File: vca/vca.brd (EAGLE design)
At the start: 35.5 x 107.6 mm, 44 parts, among them IC1 OPA4130U, IC2 OPA134D, IC3 OPA2134D, X1 2516-

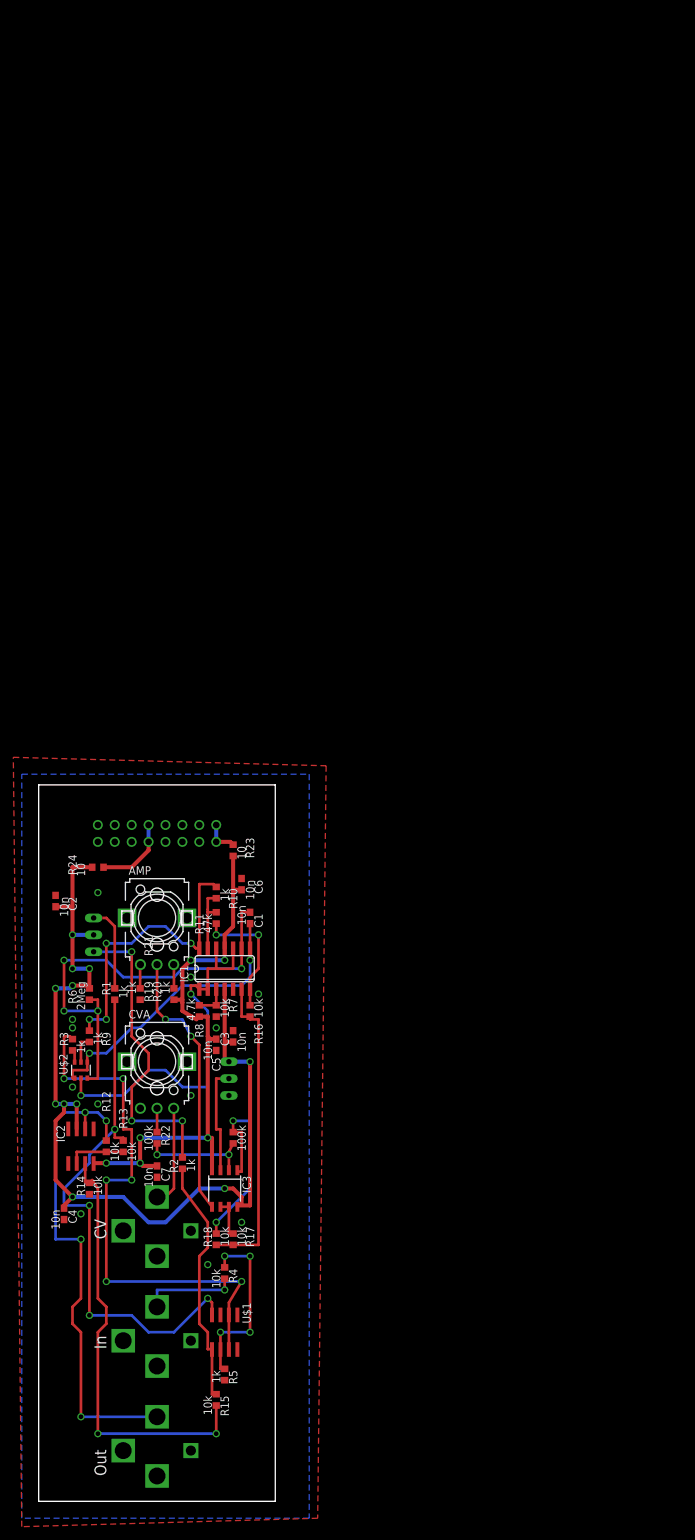
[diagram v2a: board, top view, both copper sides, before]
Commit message: changed the vca to be a 2 board design with a mixer for the input.q
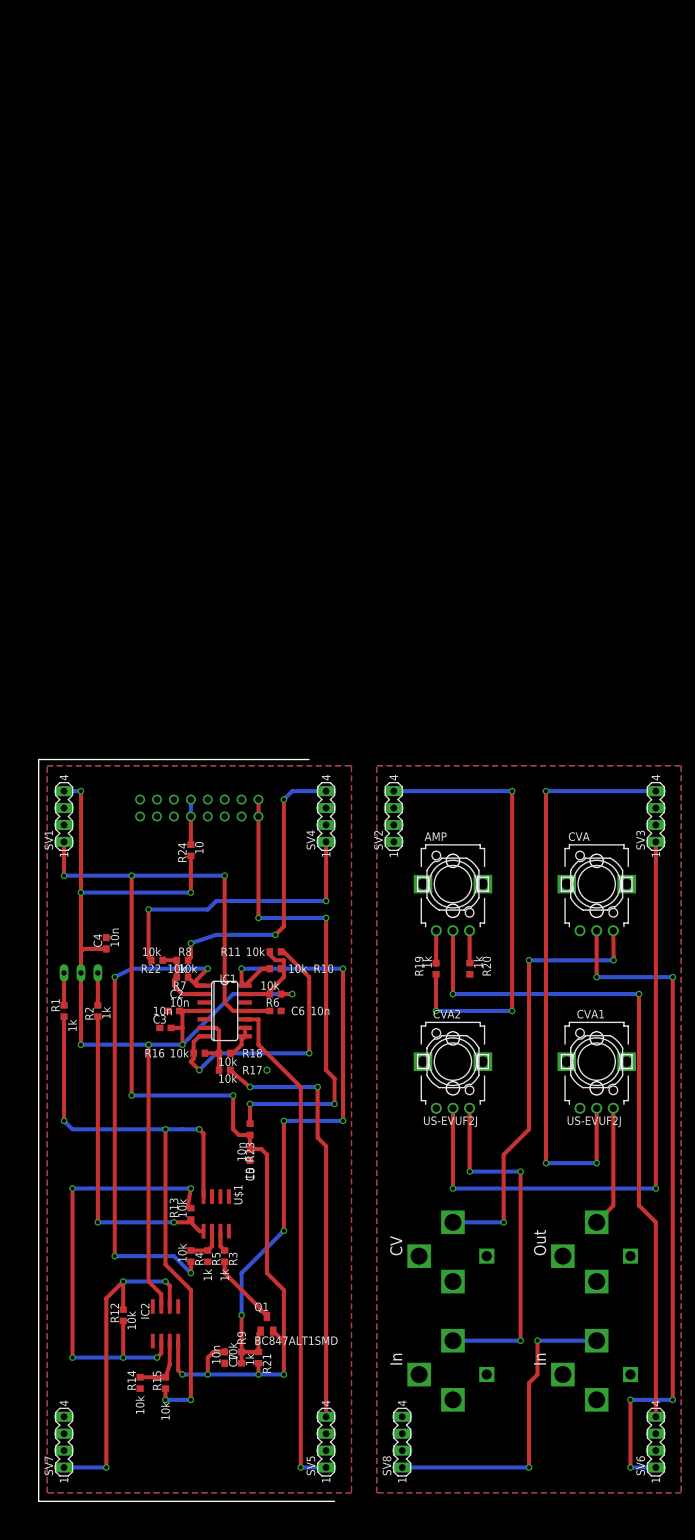
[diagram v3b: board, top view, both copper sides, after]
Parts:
- removed C1: 10n, dan:C0603
- removed IC3: OPA2134D, dan:SOIC8
- removed IN: PJ301BM, dan:PJ301BM
- removed RESP: 10k, dan:RJ9W
- removed U$2: BCM847, dan:SOT457R_PHILIPS
- added CVA1, CVA2: US-EVUF2J, dan:EVUFXJ
- added IN1, IN2: PJ301BM, dan:PJ301BM
- added Q1: BC847ALT1SMD, dan:SOT23
- added SV1, SV2, SV3, SV4, SV5, SV6, SV7, SV8: (no value), dan:MA04-1
- R10, R9: value 1k -> 10k
- R11: value 47k -> 10k
- R21: value 100k -> 1k
- R22: value 100k -> 10k
- R6: value 2Meg -> 10k
- R8: value 4.7k -> 10k
- moved CVA 71.2 mm to (82.5, 92.7)
- moved OUT 67.0 mm to (82.5, 19.1)
- moved R9 53.4 mm to (29.2, 21.6), turned to 270 degrees
- moved AMP 44.7 mm to (61.0, 92.7)
- moved CVIN 44.6 mm to (61.0, 36.8)
- moved R19 44.6 mm to (58.4, 80.0)
- moved R20 44.6 mm to (63.5, 80.0)
- moved R23 42.0 mm to (30.5, 55.9)
- moved C4 41.1 mm to (8.89, 83.8), turned to 90 degrees
- moved R3 39.1 mm to (26.7, 36.8)
- moved R21 33.2 mm to (31.8, 21.6), turned to 270 degrees
- moved R14 30.2 mm to (14.0, 17.8)
- moved C7 29.7 mm to (26.7, 21.6)
- moved IC2 29.5 mm to (17.8, 26.7)
- moved R18 28.0 mm to (26.7, 67.3), turned to 0 degrees
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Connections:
- removed net NEG8: IC1.1, IC1.10, IC1.12, IC1.2, U$2.2
- new net N$29: R22.2, SV4.1
- new net N$31: CVA.2, SV6.1
- new net N$32: AMP.2, SV6.4
- new net N$33: IC1.10, SV5.1
- net +12V: now also R19.1, R6.1, SV1.4, SV2.4; no longer IC3.8, R6.2, RESP.A
- net -12V: now also Q1.2, R21.2, SV1.1, SV2.1; no longer IC3.4, R20.2, R8.2
- net GND: now also CVA1.1, CVA2.1, IC1.12, IC1.3, R20.2, SV1.2, SV1.3, SV2.2, SV2.3, SV3.2, SV3.3, SV4.2, SV4.3, SV5.2, SV5.3, SV6.2, SV6.3, SV7.2, SV7.3, SV7.4, SV8.2, SV8.3, SV8.4; no longer IN.P$1, IN.P$2, IN.P$4, OUT.P$2, R19.1, R7.1, RESP.E
- net N$10: now also IC1.2, R22.1; no longer IC1.3
- net N$11: now also IC1.1, R7.1; no longer IN.P$3
- net N$12: now also R6.2
- net N$18: now also SV7.1; no longer OUT.P$3
- net N$19: now also CVA2.2, SV3.1; no longer IC3.6, IC3.7, R17.2
- net N$21: now also CVA1.2, SV3.4; no longer AMP.2, IC3.5
- net N$24: now also R17.2, SV5.4; no longer IC3.3, RESP.S
- net N$25: now also CVA1.3, IN1.P$3; no longer IC3.2, R21.1, R22.2
- net N$27: now also CVA2.3, IN2.P$3; no longer IC3.1, R18.2, R21.2
- net N$28: now also R8.2, SV4.4; no longer CVA.2, R22.1
- net N$3: now also R13.2; no longer R15.1
- net N$4: now also R15.1; no longer R13.2
- net N$5: now also OUT.P$3, SV8.1; no longer C1.2, IC1.8, U$2.1, U$2.4
- net N$6: now also IC1.8, IC1.9, R18.2; no longer R3.1, U$2.6
- net N$7: now also Q1.3, R3.1; no longer C1.1, IC1.9, R6.1, U$2.3
- net N$8: now also Q1.1, R21.1; no longer U$2.5
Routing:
- net N$31: track 0.00 -> 102.2 mm, vias 0 -> 5
- net N$32: track 0.00 -> 102.0 mm, vias 0 -> 2
- net -12V: track 85.7 -> 180.6 mm, vias 6 -> 9
- net N$19: track 5.93 -> 94.6 mm, vias 0 -> 2
- net N$1: track 83.3 -> 3.16 mm, vias 6 -> 0
- net N$33: track 0.00 -> 75.8 mm, vias 0 -> 1
- net +12V: track 148.3 -> 221.7 mm, vias 11 -> 10
- net N$30: track 5.25 -> 72.1 mm, vias 0 -> 4
- net N$11: track 14.4 -> 76.5 mm, vias 1 -> 4
- net N$16: track 8.73 -> 67.3 mm, vias 0 -> 5
- net NEG8: track 56.4 -> 0.00 mm, vias 2 -> 0
- net N$13: track 65.5 -> 9.35 mm, vias 2 -> 0
- net N$7: track 65.5 -> 10.8 mm, vias 4 -> 0
- net N$26: track 15.1 -> 65.7 mm, vias 0 -> 3
- net N$9: track 44.4 -> 93.5 mm, vias 4 -> 6
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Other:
- board size 35.5 x 107.6 mm -> 44.4 x 111.4 mm

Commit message: finished the vca.  more or less ready.
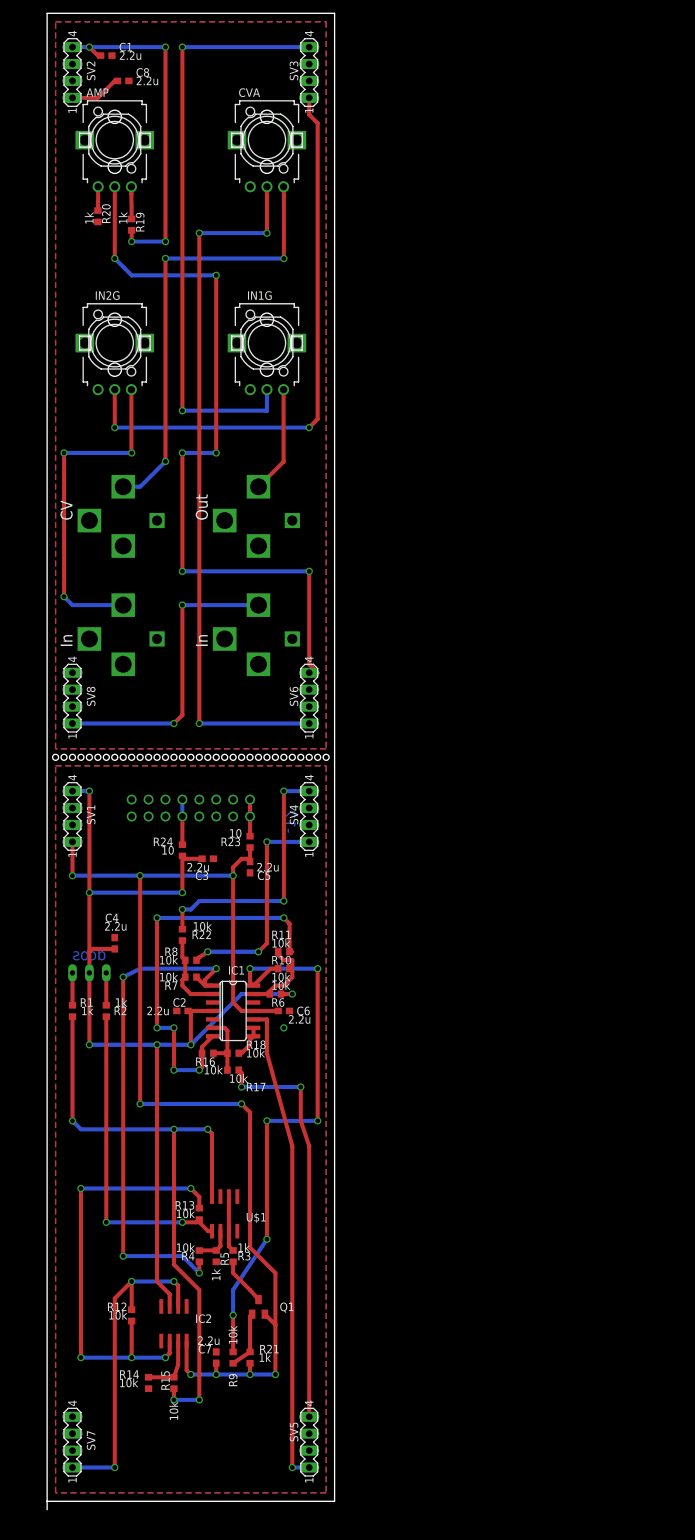
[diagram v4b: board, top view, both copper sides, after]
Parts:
- removed CVA1, CVA2: US-EVUF2J, dan:EVUFXJ
- added C1, C8: 2.2u, dan:C0603
- added IN1G, IN2G: US-EVUF2J, dan:EVUFXJ
- C2, C3, C4, C5, C6, C7: value 10n -> 2.2u
- moved R20 126.1 mm to (7.62, 193.0)
- moved SV6 123.3 mm to (39.4, 120.7)
- moved SV3 123.3 mm to (39.4, 214.6)
- moved AMP 122.8 mm to (10.2, 204.5)
- moved SV8 122.2 mm to (3.81, 120.7)
- moved CVA 122.2 mm to (33.0, 204.5)
- moved SV2 121.7 mm to (3.81, 214.6)
- moved IN1 121.6 mm to (31.8, 147.3)
- moved OUT 121.6 mm to (31.8, 129.5)
- moved CVIN 121.1 mm to (11.4, 147.3)
- moved IN2 121.1 mm to (11.4, 129.5)
- moved R19 120.8 mm to (12.7, 191.8)
- moved C5 43.2 mm to (30.5, 95.2)
- moved R23 43.2 mm to (30.5, 99.1)
- moved C3 26.2 mm to (24.1, 96.5), turned to 0 degrees
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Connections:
- net +12V: now also C1.1
- net -12V: now also C8.1
- net GND: now also C1.2, C8.2, IN1G.1, IN2G.1; no longer CVA1.1, CVA2.1
- net N$19: now also IN2G.2; no longer CVA2.2
- net N$21: now also IN1G.2; no longer CVA1.2
- net N$22: now also AMP.3; no longer AMP.1
- net N$23: now also AMP.1; no longer AMP.3
- net N$25: now also IN1G.3; no longer CVA1.3
- net N$27: now also IN2G.3; no longer CVA2.3
- net N$28: now also SV4.1; no longer SV4.4
- net N$29: now also SV4.4; no longer SV4.1
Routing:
- net N$30: track 72.1 -> 5.50 mm, vias 4 -> 0
- net N$17: track 41.7 -> 60.8 mm, vias 2 -> 6
- net +12V: track 221.7 -> 203.8 mm, vias 10 -> 11
- net N$32: track 102.0 -> 112.7 mm, vias 2 -> 6
- net N$28: track 43.3 -> 33.1 mm
- net N$9: track 93.5 -> 84.4 mm
- net N$19: track 94.6 -> 85.5 mm
- net -12V: track 180.6 -> 185.9 mm
- net N$1: track 3.16 -> 8.36 mm
- net N$31: track 102.2 -> 107.3 mm, vias 5 -> 3
- net N$29: track 43.9 -> 39.0 mm, vias 2 -> 3
- net N$7: track 10.8 -> 7.20 mm
- net N$33: track 75.8 -> 72.4 mm
- net N$8: track 5.80 -> 8.86 mm
- net N$24: track 64.1 -> 61.3 mm
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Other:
- board size 44.4 x 111.4 mm -> 43.2 x 224.8 mm
- board text added: "-12"
- board text added: "dcos"

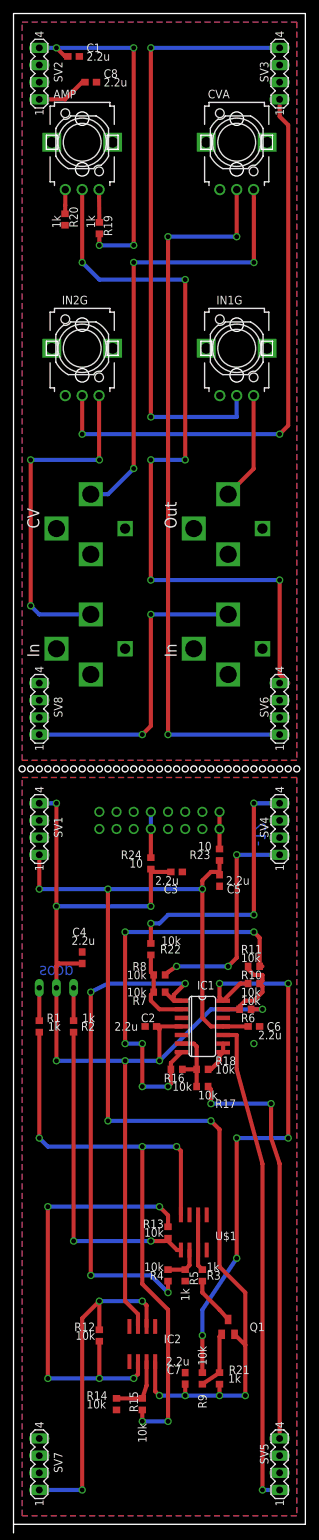
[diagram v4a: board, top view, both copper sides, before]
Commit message: finished vca.  probably needs a series protection resistor on output.
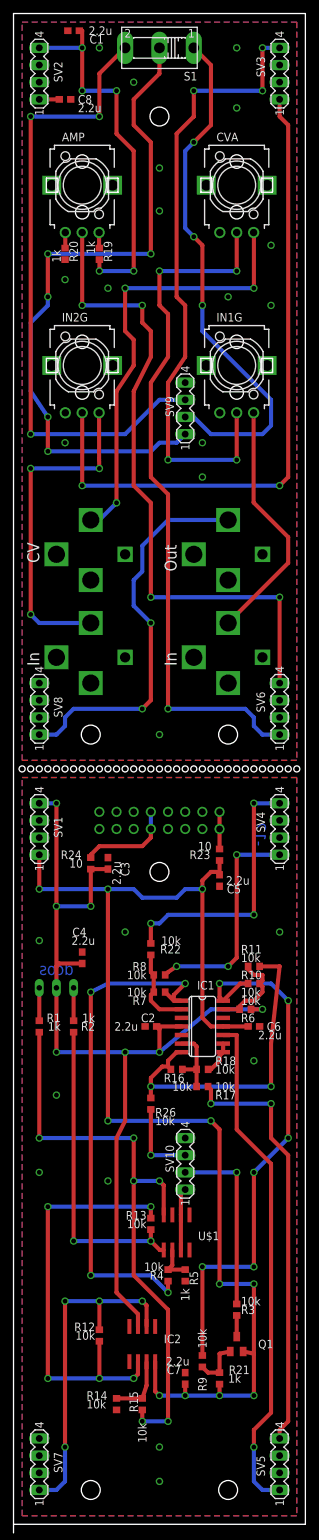
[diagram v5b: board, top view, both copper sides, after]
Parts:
- added R26: 10k, dan:R0603
- added S1: (no value), dan:255SB
- added SV10, SV9: (no value), dan:MA04-1
- R3: value 1k -> 10k
- moved IN1 19.0 mm to (31.8, 128.3)
- moved OUT 14.0 mm to (31.8, 143.5)
- moved C3 10.2 mm to (14.0, 97.8), turned to 90 degrees
- moved R24 8.89 mm to (11.4, 97.8)
- moved R3 7.18 mm to (33.0, 31.8)
- moved AMP 6.35 mm to (10.2, 198.1)
- moved CVA 6.35 mm to (33.0, 198.1)
- moved R20 5.08 mm to (7.62, 188.0)
- moved C8 4.58 mm to (7.62, 210.8)
- moved C1 3.81 mm to (8.89, 221.0), turned to 180 degrees
- moved CVIN 3.81 mm to (11.4, 143.5)
- moved R19 3.81 mm to (12.7, 188.0)
- moved Q1 2.84 mm to (33.0, 26.7)
- moved R13 2.84 mm to (20.3, 44.5)
- moved IN1G 2.54 mm to (33.0, 171.4)
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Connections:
- removed net N$17: IC1.7, R11.2, R16.1
- new net N$35: R3.2, SV10.2
- new net N$36: IC1.7, R11.2, R16.1, R26.1
- new net N$37: S1.2, SV9.1
- new net N$38: R26.2, SV10.3
- new net N$40: S1.1, SV9.2
- new net N$41: S1.3, SV9.3
- net GND: now also SV10.4, SV9.4
- net N$1: now also SV10.1; no longer R3.2
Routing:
- net N$37: track 0.00 -> 100.8 mm, vias 0 -> 5
- net N$41: track 0.00 -> 93.9 mm, vias 0 -> 3
- net N$40: track 0.00 -> 78.0 mm, vias 0 -> 3
- net N$17: track 60.8 -> 0.00 mm, vias 6 -> 0
- net N$36: track 0.00 -> 48.8 mm, vias 0 -> 2
- net N$35: track 0.00 -> 27.1 mm, vias 0 -> 1
- net N$25: track 16.2 -> 36.9 mm
- net N$32: track 112.7 -> 96.8 mm, vias 6 -> 4
- net N$5: track 45.0 -> 58.1 mm
- net N$19: track 85.5 -> 98.2 mm
- net N$38: track 0.00 -> 11.9 mm, vias 0 -> 1
- net +12V: track 203.8 -> 196.1 mm, vias 11 -> 12
- net N$34: track 6.77 -> 14.2 mm
- net N$4: track 94.6 -> 88.2 mm, vias 5 -> 6
- net N$31: track 107.3 -> 103.1 mm
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
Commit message: made a couple post fab vca changes
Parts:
- added R25: 1Meg, dan:R0603
- moved C6 13.1 mm to (29.2, 85.1), turned to 90 degrees
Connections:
- net GND: now also IN1.P$1, IN1.P$2, IN1.P$4, IN2.P$1, IN2.P$2, IN2.P$4, R25.1
- net N$12: now also R25.2
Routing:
- net N$12: track 12.9 -> 16.1 mm
- net -12V: track 186.2 -> 184.0 mm
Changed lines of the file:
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@@
 <attribute name="VALUE" x="34.925" y="95.885" size="1.27" layer="21" font="vector" ratio="15" rot="R180"/>
 </element>
-<element name="C6" library="dan" package="C0603" value="2.2u" x="35.56" y="73.66" smashed="yes">
-<attribute name="NAME" x="37.465" y="73.025" size="1.27" layer="21" font="vector" ratio="15"/>
-<attribute name="VALUE" x="36.195" y="71.755" size="1.27" layer="21" font="vector" ratio="15"/>
+<element name="C6" library="dan" package="C0603" value="2.2u" x="29.21" y="85.09" smashed="yes" rot="R90">
+<attribute name="NAME" x="29.845" y="86.995" size="1.27" layer="21" font="vector" ratio="15"/>
+<attribute name="VALUE" x="29.845" y="85.725" size="1.27" layer="21" font="vector" ratio="15"/>
 </element>
 <element name="C7" library="dan" package="C0603" value="2.2u" x="25.4" y="21.59" smashed="yes" rot="R90">
@@
 <attribute name="NAME" x="23.749" y="52.07" size="1.27" layer="21" font="vector" ratio="15" rot="R90"/>
 <attribute name="VALUE" x="23.749" y="53.975" size="1.27" layer="27" ratio="10" rot="R90"/>
+</element>
+<element name="R25" library="dan" package="R0603" value="1Meg" x="35.56" y="73.66" smashed="yes" rot="R180">
+<attribute name="NAME" x="33.655" y="71.755" size="1.27" layer="21" font="vector" ratio="15"/>
+<attribute name="VALUE" x="33.655" y="70.485" size="1.27" layer="21" font="vector" ratio="15"/>
 </element>
 </elements>
@@
 <via x="13.97" y="182.88" extent="1-16" drill="0.7"/>
 <via x="27.94" y="154.94" extent="1-16" drill="0.7"/>
+<contactref element="IN1" pad="P$4"/>
+<contactref element="IN1" pad="P$2"/>
+<contactref element="IN1" pad="P$1"/>
+<contactref element="IN2" pad="P$4"/>
+<contactref element="IN2" pad="P$1"/>
+<contactref element="IN2" pad="P$2"/>
+<contactref element="R25" pad="1"/>
 <wire x1="22.86" y1="105.41" x2="21.59" y2="116.84" width="0" layer="19" extent="1-1"/>
 </signal>
@@
 <via x="25.4" y="19.05" extent="1-16" drill="0.7"/>
 <wire x1="25.4" y1="19.05" x2="30.48" y2="19.05" width="0.6096" layer="16"/>
-<wire x1="31.0134" y1="73.66" x2="34.71" y2="73.66" width="0.6096" layer="1"/>
 <wire x1="31.0134" y1="73.66" x2="29.21" y2="73.66" width="0.6096" layer="1"/>
 <wire x1="29.21" y1="73.66" x2="27.94" y2="74.93" width="0.6096" layer="1"/>
-<wire x1="27.94" y1="74.93" x2="27.94" y2="93.98" width="0.6096" layer="1"/>
+<wire x1="27.94" y1="74.93" x2="27.94" y2="83.82" width="0.6096" layer="1"/>
 <via x="27.94" y="93.98" extent="1-16" drill="0.7"/>
 <via x="3.81" y="93.98" extent="1-16" drill="0.7"/>
+<wire x1="27.94" y1="83.82" x2="27.94" y2="93.98" width="0.6096" layer="1"/>
 <wire x1="13.97" y1="93.98" x2="3.81" y2="93.98" width="0.6096" layer="16"/>
 <wire x1="3.81" y1="93.98" x2="3.81" y2="99.06" width="0.6096" layer="1"/>
@@
 <wire x1="24.13" y1="92.71" x2="25.4" y2="93.98" width="0.6096" layer="16"/>
 <wire x1="25.4" y1="93.98" x2="27.94" y2="93.98" width="0.6096" layer="16"/>
+<wire x1="29.21" y1="84.24" x2="28.36" y2="84.24" width="0.6096" layer="1"/>
+<wire x1="28.36" y1="84.24" x2="27.94" y2="83.82" width="0.6096" layer="1"/>
 <wire x1="3.81" y1="99.06" x2="3.81" y2="210.82" width="0" layer="19" extent="1-1"/>
 </signal>
@@
 <wire x1="34.29" y1="77.47" x2="35.56" y2="77.47" width="0.6096" layer="1"/>
 <wire x1="35.56" y1="77.47" x2="36.83" y2="78.74" width="0.6096" layer="1"/>
+<contactref element="R25" pad="2"/>
+<wire x1="34.71" y1="73.66" x2="34.29" y2="73.66" width="0.6096" layer="1"/>
+<wire x1="34.29" y1="73.66" x2="34.29" y2="74.51" width="0.6096" layer="1"/>
+<wire x1="34.29" y1="74.51" x2="33.44" y2="76.2" width="0.6096" layer="1"/>
 </signal>
 <signal name="N$11">

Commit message: vcf2 changes
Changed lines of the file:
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@@
 <contactref element="R25" pad="1"/>
 <wire x1="22.86" y1="105.41" x2="21.59" y2="116.84" width="0" layer="19" extent="1-1"/>
+<via x="15.24" y="10.16" extent="1-16" drill="0.7"/>
 </signal>
 <signal name="+12V">
